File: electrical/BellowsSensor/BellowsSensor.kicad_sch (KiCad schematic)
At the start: 5 parts, among them U1 ABPMRRV001PD2A3

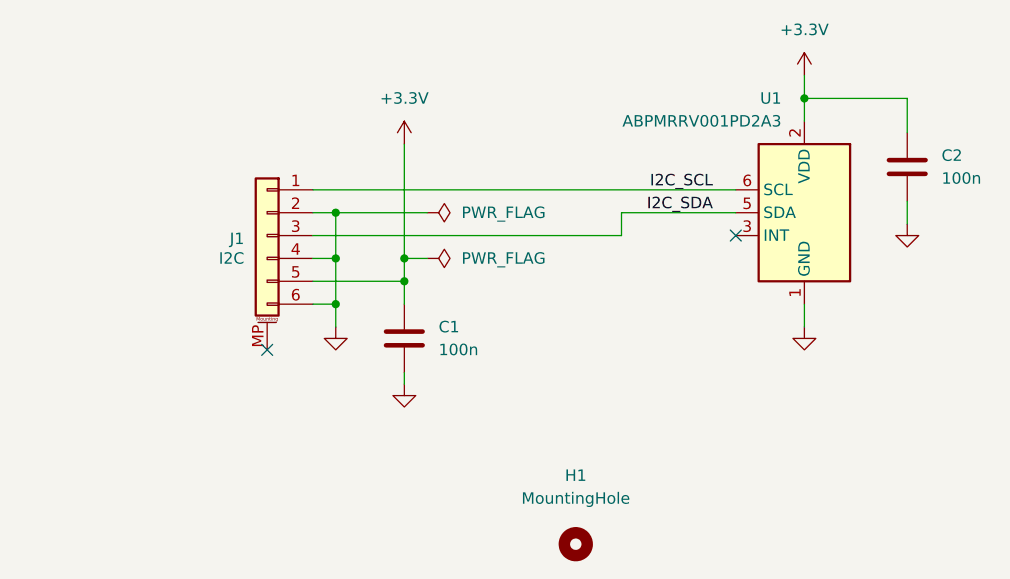
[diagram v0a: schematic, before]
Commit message: Replace pressure sensor part
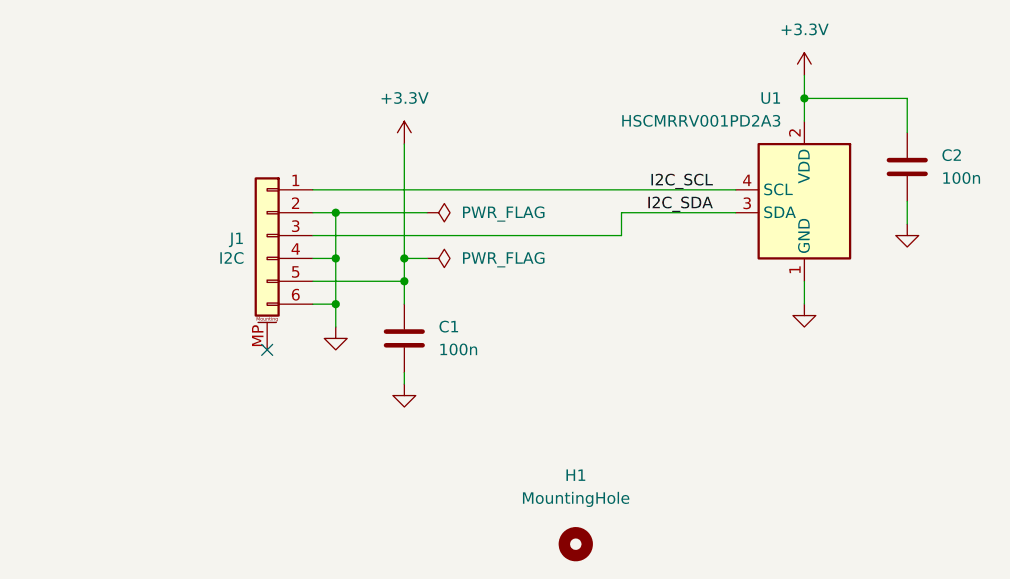
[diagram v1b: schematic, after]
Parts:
- removed U1: ABPMRRV001PD2A3, MidiConcertina:Honeywell_ABPMRRx, symbol MidiConcertina:Honeywell_ABPx2x
- added U1: HSCMRRV001PD2A3, MidiConcertina:Honeywell_HSCMRRx, symbol MidiConcertina:Honeywell_HSCx2x
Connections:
- net +3.3V: now also U1.2 (VDD)
- net GND: now also U1.1 (GND)
- net I2C_SCL: now also U1.4 (SCL)
- net I2C_SDA: now also U1.3 (SDA)
- no-connect marks 2 -> 1
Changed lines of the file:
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@@
 		(at 99.06 95.25)
 	)
-	(no_connect
-		(at 151.13 82.55)
-	)
 	(wire
 		(pts
@@
 	(wire
 		(pts
-			(xy 158.75 92.71) (xy 158.75 90.17)
+			(xy 158.75 90.17) (xy 158.75 87.63)
 		)
 		(stroke
@@
 	(symbol
 		(lib_id "power:GND")
-		(at 158.75 92.71 0)
+		(at 158.75 90.17 0)
 		(mirror y)
 		(unit 1)
@@
 		(fields_autoplaced yes)
 		(property "Reference" "#PWR05"
-			(at 158.75 99.06 0)
+			(at 158.75 96.52 0)
 			(effects
 				(font
@@
 		)
 		(property "Value" "GND"
-			(at 158.75 97.79 0)
+			(at 158.75 95.25 0)
 			(effects
 				(font
@@
 		)
 		(property "Footprint" ""
-			(at 158.75 92.71 0)
+			(at 158.75 90.17 0)
 			(effects
 				(font
@@
 		)
 		(property "Datasheet" ""
-			(at 158.75 92.71 0)
+			(at 158.75 90.17 0)
 			(effects
 				(font
@@
 		)
 		(property "Description" "Power symbol creates a global label with name \"GND\" , ground"
-			(at 158.75 92.71 0)
+			(at 158.75 90.17 0)
 			(effects
 				(font
@@
 	)
 	(symbol
+		(lib_id "MidiConcertina:Honeywell_HSCx2x")
+		(at 158.75 80.01 0)
+		(mirror y)
+		(unit 1)
+		(exclude_from_sim no)
+		(in_bom yes)
+		(on_board yes)
+		(dnp no)
+		(property "Reference" "U1"
+			(at 156.21 67.31 0)
+			(effects
+				(font
+					(size 1.27 1.27)
+				)
+				(justify left)
+			)
+		)
+		(property "Value" "HSCMRRV001PD2A3"
+			(at 156.21 69.85 0)
+			(effects
+				(font
+					(size 1.27 1.27)
+				)
+				(justify left)
+			)
+		)
+		(property "Footprint" "MidiConcertina:Honeywell_HSCMRRx"
+			(at 158.75 80.01 0)
+			(effects
+				(font
+					(size 1.27 1.27)
+				)
+				(hide yes)
+			)
+		)
+		(property "Datasheet" "https://prod-edam.honeywell.com/content/dam/honeywell-edam/sps/siot/en-us/products/sensors/pressure-sensors/board-mount-pressure-sensors/trustability-hsc-series/documents/sps-siot-trustability-hsc-series-high-accuracy-board-mount-pressure-sensors-50099148-a-en-ciid-151133.pdf"
+			(at 158.75 80.01 0)
+			(effects
+				(font
+					(size 1.27 1.27)
+				)
+				(hide yes)
+			)
+		)
+		(property "Description" "Pressure Sensor ±1PSI (±6.89kPa) Differential Male - 0.06\" (1.6mm) Tube, Dual Ports, Same Side, ROHS"
+			(at 158.75 80.01 0)
+			(effects
+				(font
+					(size 1.27 1.27)
+				)
+				(hide yes)
+			)
+		)
+		(property "LCSC" "C21442059"
+			(at 158.75 80.01 0)
+			(effects
+				(font
+					(size 1.27 1.27)
+				)
+				(hide yes)
+			)
+		)
+		(property "Part" "Honeywell ABPMRRV001PD2A3"
+			(at 158.75 80.01 0)
+			(effects
+				(font
+					(size 1.27 1.27)
+				)
+				(hide yes)
+			)
+		)
+		(pin "4"
+		)
+		(pin "2"
+		)
+		(pin "1"
+		)
+		(pin "8"
+		)
+		(pin "7"
+		)
+		(pin "5"
+		)
+		(pin "6"
+		)
+		(pin "3"
+		)
+		(instances
+			(project ""
+				(path "/ceae7089-9cb4-4950-bb64-2f75302207fd"
+					(reference "U1")
+					(unit 1)
+				)
+			)
+		)
+	)
+	(symbol
 		(lib_id "Mechanical:MountingHole")
 		(at 133.35 116.84 0)
@@
 					(unit 1)
 				)
-			)
-		)
-	)
-	(symbol
-		(lib_id "MidiConcertina:Honeywell_ABPx2x")
-		(at 158.75 80.01 0)
-		(mirror y)
-		(unit 1)
-		(exclude_from_sim no)
-		(in_bom yes)
-		(on_board yes)
-		(dnp no)
-		(property "Reference" "U1"
-			(at 156.21 67.31 0)
-			(effects
-				(font
-					(size 1.27 1.27)
-				)
-				(justify left)
-			)
-		)
-		(property "Value" "ABPMRRV001PD2A3"
-			(at 156.21 69.85 0)
-			(effects
-				(font
-					(size 1.27 1.27)
-				)
-				(justify left)
-			)
-		)
-		(property "Footprint" "MidiConcertina:Honeywell_ABPMRRx"
-			(at 158.75 80.01 0)
-			(effects
-				(font
-					(size 1.27 1.27)
-				)
-				(hide yes)
-			)
-		)
-		(property "Datasheet" "https://prod-edam.honeywell.com/content/dam/honeywell-edam/sps/siot/en-us/products/sensors/pressure-sensors/board-mount-pressure-sensors/basic-abp-series/documents/sps-siot-basic-board-mount-pressure-abp-series-datasheet-32305128-ciid-155789.pdf"
-			(at 158.75 80.01 0)
-			(effects
-				(font
-					(size 1.27 1.27)
-				)
-				(hide yes)
-			)
-		)
-		(property "Description" "Pressure Sensor ±1PSI (±6.89kPa) Differential Male - 0.06\" (1.6mm) Tube, Dual Ports, Same Side, ROHS"
-			(at 158.75 80.01 0)
-			(effects
-				(font
-					(size 1.27 1.27)
-				)
-				(hide yes)
-			)
-		)
-		(property "LCSC" ""
-			(at 158.75 80.01 0)
-			(effects
-				(font
-					(size 1.27 1.27)
-				)
-				(hide yes)
-			)
-		)
-		(property "Part" "Honeywell ABPMRRV001PD2A3"
-			(at 158.75 80.01 0)
-			(effects
-				(font
-					(size 1.27 1.27)
-				)
-				(hide yes)
-			)
-		)
-		(property "Note" ""
-			(at 158.75 80.01 0)
-			(effects
-				(font
-					(size 1.27 1.27)
-				)
-			)
-		)
-		(property "Tolerance" ""
-			(at 158.75 80.01 0)
-			(effects
-				(font
-					(size 1.27 1.27)
-				)
-			)
-		)
-		(pin "5"
-		)
-		(pin "3"
-		)
-		(pin "1"
-		)
-		(pin "2"
-		)
-		(pin "6"
-		)
-		(pin "4"
-		)
-		(instances
-			(project "BellowsSensor"
-				(path "/ceae7089-9cb4-4950-bb64-2f75302207fd"
-					(reference "U1")
-					(unit 1)
-				)

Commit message: Minor corrections to bellows sensor design
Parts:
- J1: LCSC C99277 -> C17393620
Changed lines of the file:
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@@
 			)
 		)
-		(property "LCSC" "C99277"
+		(property "LCSC" "C17393620"
 			(at 99.06 82.55 0)
 			(effects

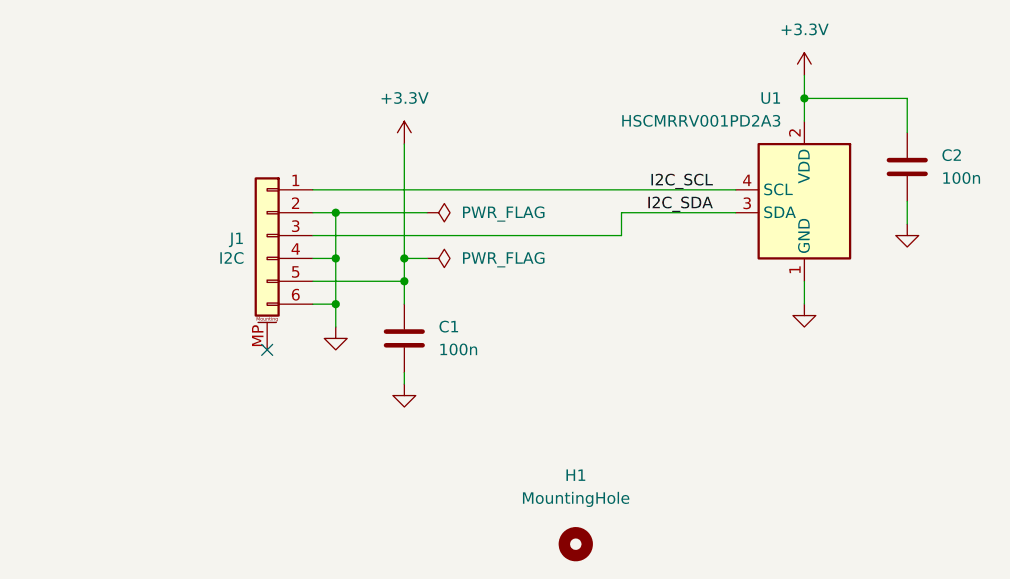
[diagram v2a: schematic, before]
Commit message: Switch pressure sensors again
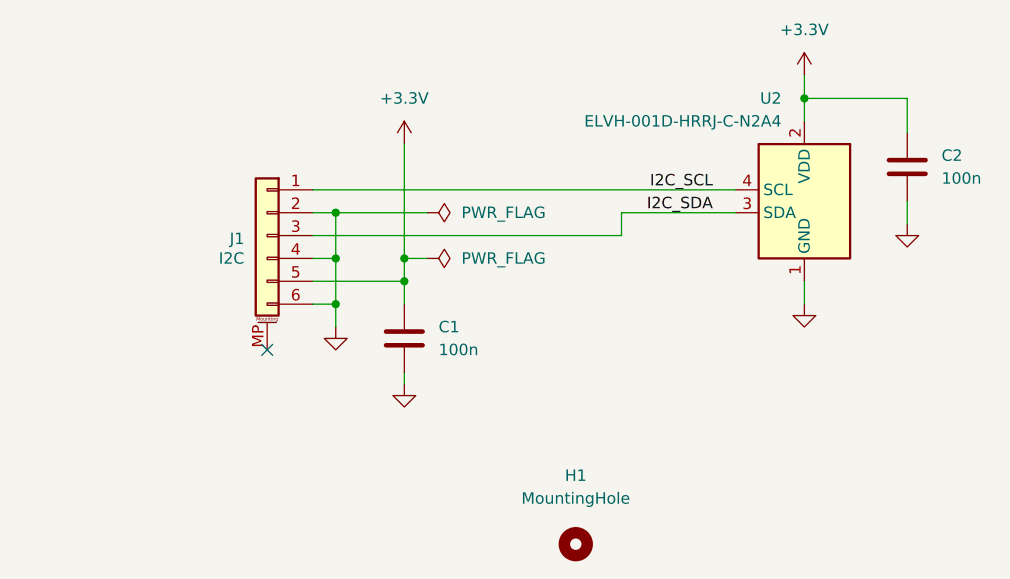
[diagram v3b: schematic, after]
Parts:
- removed U1: HSCMRRV001PD2A3, MidiConcertina:Honeywell_HSCMRRx, symbol MidiConcertina:Honeywell_HSCx2x
- added U2: ELVH-001D-HRRJ-C-N2A4, MidiConcertina:Amphenol_ELVH-x-xJ-x-x, symbol MidiConcertina:Amphenol_ELVH-x
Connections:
- net +3.3V: now also U2.2 (VDD)
- net GND: now also U2.1 (GND)
- net I2C_SCL: now also U2.4 (SCL)
- net I2C_SDA: now also U2.3 (SDA)
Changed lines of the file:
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@@
+	)
+	(symbol
+		(lib_id "MidiConcertina:Amphenol_ELVH-x")
+		(at 158.75 80.01 0)
+		(mirror y)
+		(unit 1)
+		(exclude_from_sim no)
+		(in_bom yes)
+		(on_board yes)
+		(dnp no)
+		(property "Reference" "U2"
+			(at 156.21 67.31 0)
+			(effects
+				(font
+					(size 1.27 1.27)
+				)
+				(justify left)
+			)
+		)
+		(property "Value" "ELVH-001D-HRRJ-C-N2A4"
+			(at 156.21 69.85 0)
+			(effects
+				(font
+					(size 1.27 1.27)
+				)
+				(justify left)
+			)
+		)
+		(property "Footprint" "MidiConcertina:Amphenol_ELVH-x-xJ-x-x"
+			(at 158.75 80.01 0)
+			(effects
+				(font
+					(size 1.27 1.27)
+				)
+				(hide yes)
+			)
+		)
+		(property "Datasheet" "https://428059.fs1.hubspotusercontent-na1.net/hubfs/428059/Product-Data-Sheets/DS-0376.pdf"
+			(at 158.75 80.01 0)
+			(effects
+				(font
+					(size 1.27 1.27)
+				)
+				(hide yes)
+			)
+		)
+		(property "Description" "Pressure Sensor ±1PSI (±6.89kPa) Differential Male - 0.06\" (1.6mm) Tube, Dual Ports, Same Side, ROHS"
+			(at 158.75 80.01 0)
+			(effects
+				(font
+					(size 1.27 1.27)
+				)
+				(hide yes)
+			)
+		)
+		(property "LCSC" "C3241336"
+			(at 158.75 80.01 0)
+			(effects
+				(font
+					(size 1.27 1.27)
+				)
+				(hide yes)
+			)
+		)
+		(property "Part" "Amphenol ELVH-001D-HRRJ-C-N2A4"
+			(at 158.75 80.01 0)
+			(effects
+				(font
+					(size 1.27 1.27)
+				)
+				(hide yes)
+			)
+		)
+		(pin "8"
+		)
+		(pin "4"
+		)
+		(pin "1"
+		)
+		(pin "3"
+		)
+		(pin "6"
+		)
+		(pin "7"
+		)
+		(pin "2"
+		)
+		(pin "5"
+		)
+		(instances
+			(project ""
+				(path "/ceae7089-9cb4-4950-bb64-2f75302207fd"
+					(reference "U2")
+					(unit 1)
+				)
+			)
+		)
 	)
 	(symbol
@@
 					(unit 1)
 				)
-			)
-		)
-	)
-	(symbol
-		(lib_id "MidiConcertina:Honeywell_HSCx2x")
-		(at 158.75 80.01 0)
-		(mirror y)
-		(unit 1)
-		(exclude_from_sim no)
-		(in_bom yes)
-		(on_board yes)
-		(dnp no)
-		(property "Reference" "U1"
-			(at 156.21 67.31 0)
-			(effects
-				(font
-					(size 1.27 1.27)
-				)
-				(justify left)
-			)
-		)
-		(property "Value" "HSCMRRV001PD2A3"
-			(at 156.21 69.85 0)
-			(effects
-				(font
-					(size 1.27 1.27)
-				)
-				(justify left)
-			)
-		)
-		(property "Footprint" "MidiConcertina:Honeywell_HSCMRRx"
-			(at 158.75 80.01 0)
-			(effects
-				(font
-					(size 1.27 1.27)
-				)
-				(hide yes)
-			)
-		)
-		(property "Datasheet" "https://prod-edam.honeywell.com/content/dam/honeywell-edam/sps/siot/en-us/products/sensors/pressure-sensors/board-mount-pressure-sensors/trustability-hsc-series/documents/sps-siot-trustability-hsc-series-high-accuracy-board-mount-pressure-sensors-50099148-a-en-ciid-151133.pdf"
-			(at 158.75 80.01 0)
-			(effects
-				(font
-					(size 1.27 1.27)
-				)
-				(hide yes)
-			)
-		)
-		(property "Description" "Pressure Sensor ±1PSI (±6.89kPa) Differential Male - 0.06\" (1.6mm) Tube, Dual Ports, Same Side, ROHS"
-			(at 158.75 80.01 0)
-			(effects
-				(font
-					(size 1.27 1.27)
-				)
-				(hide yes)
-			)
-		)
-		(property "LCSC" "C21442059"
-			(at 158.75 80.01 0)
-			(effects
-				(font
-					(size 1.27 1.27)
-				)
-				(hide yes)
-			)
-		)
-		(property "Part" "Honeywell ABPMRRV001PD2A3"
-			(at 158.75 80.01 0)
-			(effects
-				(font
-					(size 1.27 1.27)
-				)
-				(hide yes)
-			)
-		)
-		(pin "4"
-		)
-		(pin "2"
-		)
-		(pin "1"
-		)
-		(pin "8"
-		)
-		(pin "7"
-		)
-		(pin "5"
-		)
-		(pin "6"
-		)
-		(pin "3"
-		)
-		(instances
-			(project ""
-				(path "/ceae7089-9cb4-4950-bb64-2f75302207fd"
-					(reference "U1")
-					(unit 1)
-				)

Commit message: Replace PicoBlade connectors with SKEDD
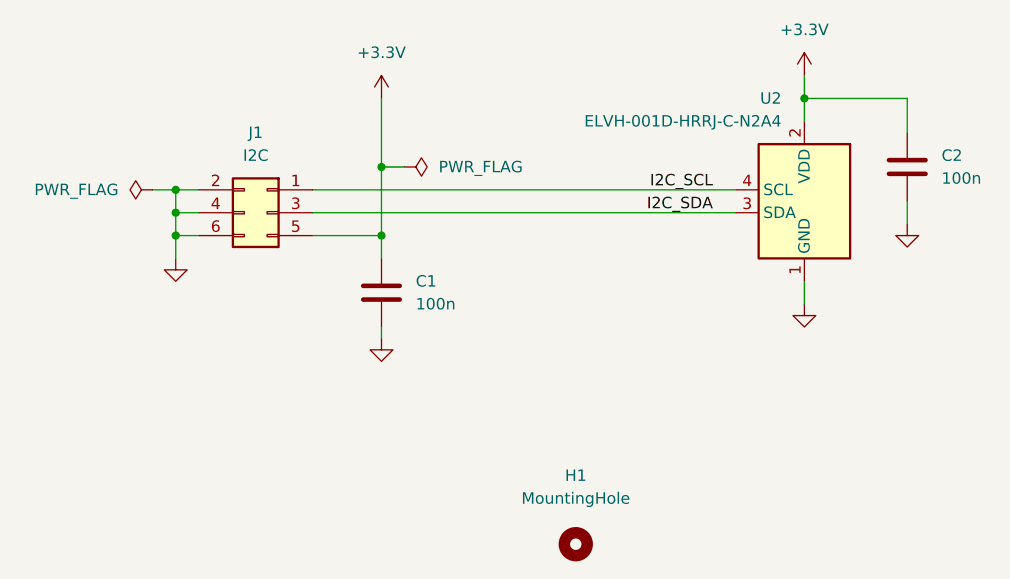
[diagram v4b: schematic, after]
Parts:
- removed J1: ~, Connector_Molex:Molex_PicoBlade_53261-0671_1x06-1MP_P1.25mm_Horizontal, symbol Connector_Generic_MountingPin:Conn_01x06_MountingPin
- added J1: I2C, MidiConcertina:Wuerth_WR-WST_490107670612_2x03_P2.54mm_SKEDD, symbol Connector_Generic:Conn_02x03_Odd_Even
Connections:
- net +3.3V: now also J1.5 (Pin_5)
- net GND: now also J1.2 (Pin_2), J1.4 (Pin_4), J1.6 (Pin_6)
- net I2C_SCL: now also J1.1 (Pin_1)
- net I2C_SDA: now also J1.3 (Pin_3)
- no-connect marks 1 -> 0
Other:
- moved on the sheet: C1

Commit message: Relabel components
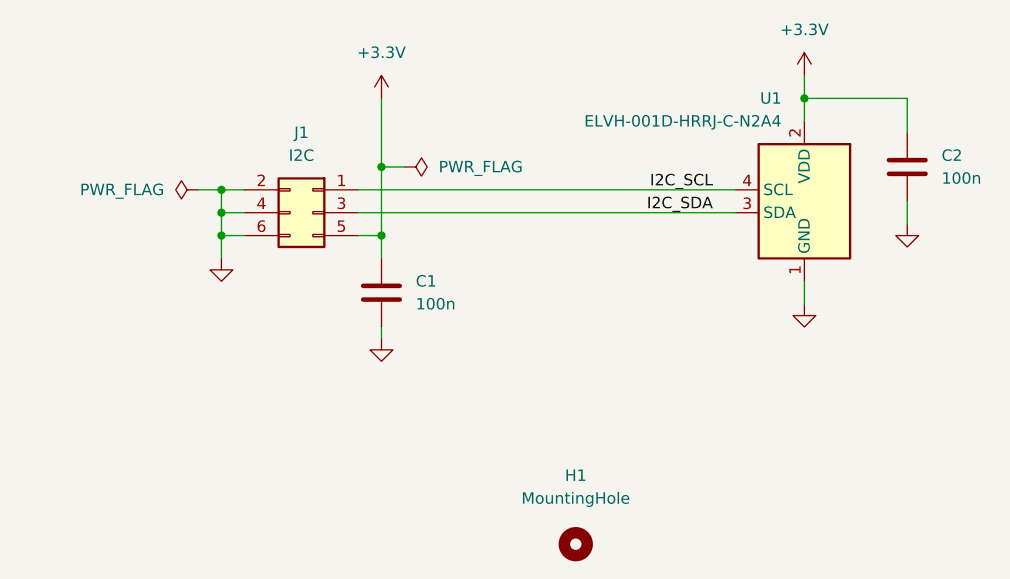
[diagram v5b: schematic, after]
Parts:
- renumbered U2 to U1
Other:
- moved on the sheet: J1
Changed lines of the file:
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@@
 	)
 	(junction
-		(at 88.9 77.47)
+		(at 93.98 77.47)
 		(diameter 0)
 		(color 0 0 0 0)
@@
 	)
 	(junction
-		(at 88.9 80.01)
+		(at 93.98 80.01)
 		(diameter 0)
 		(color 0 0 0 0)
@@
 	)
 	(junction
-		(at 88.9 82.55)
+		(at 93.98 82.55)
 		(diameter 0)
 		(color 0 0 0 0)
@@
 	(wire
 		(pts
-			(xy 88.9 80.01) (xy 88.9 82.55)
+			(xy 93.98 80.01) (xy 93.98 82.55)
 		)
 		(stroke
@@
 	(wire
 		(pts
-			(xy 104.14 77.47) (xy 151.13 77.47)
-		)
-		(stroke
-			(width 0)
-			(type default)
-		)
-	)
-	(wire
-		(pts
-			(xy 88.9 80.01) (xy 91.44 80.01)
-		)
-		(stroke
-			(width 0)
-			(type default)
-		)
-	)
-	(wire
-		(pts
-			(xy 88.9 77.47) (xy 91.44 77.47)
-		)
-		(stroke
-			(width 0)
-			(type default)
-		)
-	)
-	(wire
-		(pts
-			(xy 88.9 82.55) (xy 88.9 85.09)
+			(xy 109.22 77.47) (xy 151.13 77.47)
+		)
+		(stroke
+			(width 0)
+			(type default)
+		)
+	)
+	(wire
+		(pts
+			(xy 93.98 80.01) (xy 96.52 80.01)
+		)
+		(stroke
+			(width 0)
+			(type default)
+		)
+	)
+	(wire
+		(pts
+			(xy 93.98 77.47) (xy 96.52 77.47)
+		)
+		(stroke
+			(width 0)
+			(type default)
+		)
+	)
+	(wire
+		(pts
+			(xy 93.98 82.55) (xy 93.98 85.09)
 		)
 		(stroke
@@
 	(wire
 		(pts
-			(xy 104.14 80.01) (xy 151.13 80.01)
-		)
-		(stroke
-			(width 0)
-			(type default)
-		)
-	)
-	(wire
-		(pts
-			(xy 86.36 77.47) (xy 88.9 77.47)
+			(xy 109.22 80.01) (xy 151.13 80.01)
+		)
+		(stroke
+			(width 0)
+			(type default)
+		)
+	)
+	(wire
+		(pts
+			(xy 91.44 77.47) (xy 93.98 77.47)
 		)
 		(stroke
@@
 	(wire
 		(pts
-			(xy 88.9 77.47) (xy 88.9 80.01)
+			(xy 93.98 77.47) (xy 93.98 80.01)
 		)
 		(stroke
@@
 	(wire
 		(pts
-			(xy 91.44 82.55) (xy 88.9 82.55)
+			(xy 96.52 82.55) (xy 93.98 82.55)
 		)
 		(stroke
@@
 	(wire
 		(pts
-			(xy 104.14 82.55) (xy 111.76 82.55)
+			(xy 109.22 82.55) (xy 111.76 82.55)
 		)
 		(stroke
@@
 	(symbol
 		(lib_id "Connector_Generic:Conn_02x03_Odd_Even")
-		(at 99.06 80.01 0)
+		(at 104.14 80.01 0)
 		(mirror y)
 		(unit 1)
@@
 		(fields_autoplaced yes)
 		(property "Reference" "J1"
-			(at 97.79 71.12 0)
+			(at 102.87 71.12 0)
 			(effects
 				(font
@@
 		)
 		(property "Value" "I2C"
-			(at 97.79 73.66 0)
+			(at 102.87 73.66 0)
 			(effects
 				(font
@@
 		)
 		(property "Footprint" "MidiConcertina:Wuerth_WR-WST_490107670612_2x03_P2.54mm_SKEDD"
-			(at 99.06 80.01 0)
+			(at 104.14 80.01 0)
 			(effects
 				(font
@@
 		)
 		(property "Datasheet" ""
-			(at 99.06 80.01 0)
+			(at 104.14 80.01 0)
 			(effects
 				(font
@@
 		)
 		(property "Description" ""
-			(at 99.06 80.01 0)
+			(at 104.14 80.01 0)
 			(effects
 				(font
@@
 		(on_board yes)
 		(dnp no)
-		(property "Reference" "U2"
+		(property "Reference" "U1"
 			(at 156.21 67.31 0)
 			(effects
@@
 			(project ""
 				(path "/ceae7089-9cb4-4950-bb64-2f75302207fd"
-					(reference "U2")
+					(reference "U1")
 					(unit 1)
 				)
@@
 	(symbol
 		(lib_id "power:PWR_FLAG")
-		(at 86.36 77.47 90)
+		(at 91.44 77.47 90)
 		(unit 1)
 		(exclude_from_sim no)
@@
 		(dnp no)
 		(property "Reference" "#FLG02"
-			(at 84.455 77.47 0)
+			(at 89.535 77.47 0)
 			(effects
 				(font
@@
 		)
 		(property "Value" "PWR_FLAG"
-			(at 82.55 77.4699 90)
+			(at 87.63 77.4699 90)
 			(effects
 				(font
@@
 		)
 		(property "Footprint" ""
-			(at 86.36 77.47 0)
+			(at 91.44 77.47 0)
 			(effects
 				(font
@@
 		)
 		(property "Datasheet" "~"
-			(at 86.36 77.47 0)
+			(at 91.44 77.47 0)
 			(effects
 				(font
@@
 		)
 		(property "Description" "Special symbol for telling ERC where power comes from"
-			(at 86.36 77.47 0)
+			(at 91.44 77.47 0)
 			(effects
 				(font
@@
 	(symbol
 		(lib_id "power:GND")
-		(at 88.9 85.09 0)
+		(at 93.98 85.09 0)
 		(unit 1)
 		(exclude_from_sim no)
@@
 		(fields_autoplaced yes)
 		(property "Reference" "#PWR07"
-			(at 88.9 91.44 0)
+			(at 93.98 91.44 0)
 			(effects
 				(font
@@
 		)
 		(property "Value" "GND"
-			(at 88.9 90.17 0)
+			(at 93.98 90.17 0)
 			(effects
 				(font
@@
 		)
 		(property "Footprint" ""
-			(at 88.9 85.09 0)
+			(at 93.98 85.09 0)
 			(effects
 				(font
@@
 		)
 		(property "Datasheet" ""
-			(at 88.9 85.09 0)
+			(at 93.98 85.09 0)
 			(effects
 				(font
@@
 		)
 		(property "Description" "Power symbol creates a global label with name \"GND\" , ground"
-			(at 88.9 85.09 0)
-			(effects
-				(font
+			(at 93.98 85.09 0)
+			(effects
+				(font

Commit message: Update titles in kicad files
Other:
- title: MIDI Concertina Bellows Sensor -> MIDI Bellows Sensor
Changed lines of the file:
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@@
 	(paper "USLetter")
 	(title_block
-		(title "MIDI Concertina Bellows Sensor")
+		(title "MIDI Bellows Sensor")
 		(comment 1 "https://ohwr.org/cern_ohl_s_v2.pdf")
 		(comment 2 "Licensed under CERN-OHL-S v2 or any later version")
